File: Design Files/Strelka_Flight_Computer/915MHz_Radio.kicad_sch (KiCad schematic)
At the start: 4 parts

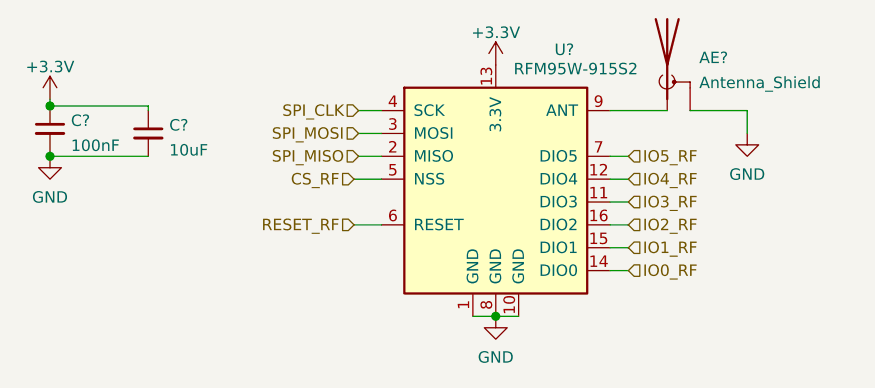
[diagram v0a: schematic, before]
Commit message: Working SPICE sim for ematch continuity circuit
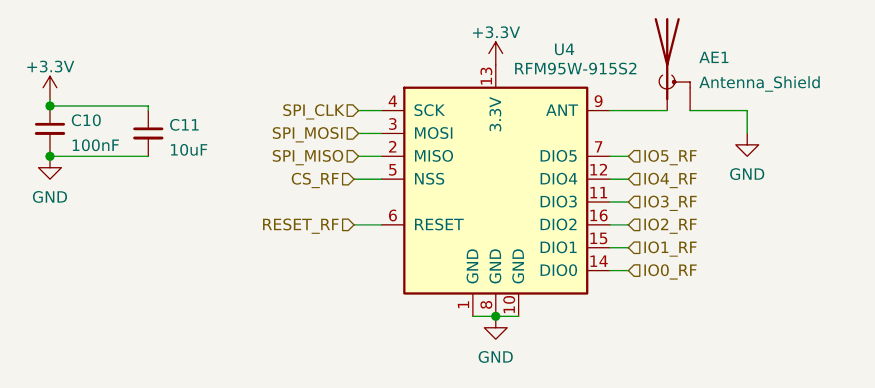
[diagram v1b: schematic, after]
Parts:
- gave numbers to parts that had none: 4
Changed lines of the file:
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@@
   (symbol (lib_id "power:GND") (at 175.26 90.805 0) (unit 1)
     (in_bom yes) (on_board yes) (fields_autoplaced)
-    (property "Reference" "#PWR?" (id 0) (at 175.26 97.155 0)
+    (property "Reference" "#PWR0125" (id 0) (at 175.26 97.155 0)
       (effects (font (size 1.27 1.27)) hide)
     )
@@
   (symbol (lib_id "RF_Module:RFM95W-915S2") (at 147.32 95.885 0) (unit 1)
     (in_bom yes) (on_board yes)
-    (property "Reference" "U?" (id 0) (at 154.94 81.5044 0))
+    (property "Reference" "U4" (id 0) (at 154.94 81.5044 0))
     (property "Value" "RFM95W-915S2" (id 1) (at 156.21 83.6445 0))
     (property "Footprint" "RF_Module:HOPERF_RFM9XW_SMD" (id 2) (at 63.5 53.975 0)
@@
   (symbol (lib_id "Device:C_Small") (at 108.712 90.805 0) (unit 1)
     (in_bom yes) (on_board yes) (fields_autoplaced)
-    (property "Reference" "C?" (id 0) (at 111.0362 89.8965 0)
+    (property "Reference" "C11" (id 0) (at 111.0362 89.8965 0)
       (effects (font (size 1.27 1.27)) (justify left))
     )
@@
   (symbol (lib_id "Device:Antenna_Shield") (at 166.37 83.185 0) (unit 1)
     (in_bom yes) (on_board yes) (fields_autoplaced)
-    (property "Reference" "AE?" (id 0) (at 169.9261 82.4035 0)
+    (property "Reference" "AE1" (id 0) (at 169.9261 82.4035 0)
       (effects (font (size 1.27 1.27)) (justify left))
     )
@@
   (symbol (lib_id "power:+3.3V") (at 147.32 83.185 0) (unit 1)
     (in_bom yes) (on_board yes) (fields_autoplaced)
-    (property "Reference" "#PWR?" (id 0) (at 147.32 86.995 0)
+    (property "Reference" "#PWR0123" (id 0) (at 147.32 86.995 0)
       (effects (font (size 1.27 1.27)) hide)
     )
@@
   (symbol (lib_id "power:+3.3V") (at 97.79 86.995 0) (unit 1)
     (in_bom yes) (on_board yes) (fields_autoplaced)
-    (property "Reference" "#PWR?" (id 0) (at 97.79 90.805 0)
+    (property "Reference" "#PWR0122" (id 0) (at 97.79 90.805 0)
       (effects (font (size 1.27 1.27)) hide)
     )
@@
   (symbol (lib_id "power:GND") (at 147.32 111.125 0) (unit 1)
     (in_bom yes) (on_board yes) (fields_autoplaced)
-    (property "Reference" "#PWR?" (id 0) (at 147.32 117.475 0)
+    (property "Reference" "#PWR0124" (id 0) (at 147.32 117.475 0)
       (effects (font (size 1.27 1.27)) hide)
     )
@@
   (symbol (lib_id "Device:C_Small") (at 97.79 90.297 0) (unit 1)
     (in_bom yes) (on_board yes) (fields_autoplaced)
-    (property "Reference" "C?" (id 0) (at 100.1142 89.3885 0)
+    (property "Reference" "C10" (id 0) (at 100.1142 89.3885 0)
       (effects (font (size 1.27 1.27)) (justify left))
     )
@@
   (symbol (lib_id "power:GND") (at 97.79 93.345 0) (unit 1)
     (in_bom yes) (on_board yes) (fields_autoplaced)
-    (property "Reference" "#PWR?" (id 0) (at 97.79 99.695 0)
+    (property "Reference" "#PWR0126" (id 0) (at 97.79 99.695 0)
       (effects (font (size 1.27 1.27)) hide)
     )

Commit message: Started component placement
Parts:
- AE1: footprint Connector_Coaxial:SMA_Amphenol_132289_EdgeMount -> Connector_Coaxial:SMA_Amphenol_132134_Vertical
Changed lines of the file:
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@@
       (effects (font (size 1.27 1.27)) (justify left))
     )
-    (property "Footprint" "Connector_Coaxial:SMA_Amphenol_132289_EdgeMount" (id 2) (at 166.37 80.645 0)
+    (property "Footprint" "Connector_Coaxial:SMA_Amphenol_132134_Vertical" (id 2) (at 166.37 80.645 0)
       (effects (font (size 1.27 1.27)) hide)
     )

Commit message: Creating BOM
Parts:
- AE1: LCSC C496550 -> (none); LCSC# (none) -> C496550
- U4: LCSC# (none) -> C2844473
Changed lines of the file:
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@@
+      (effects (font (size 1.27 1.27)) hide)
+    )
+    (property "LCSC#" "C2844473" (id 4) (at 147.32 95.885 0)
       (effects (font (size 1.27 1.27)) hide)
     )
@@
       (effects (font (size 1.27 1.27)) hide)
     )
-    (property "LCSC" "C496550" (id 4) (at 166.37 83.185 0)
+    (property "LCSC#" "C496550" (id 4) (at 166.37 83.185 0)
       (effects (font (size 1.27 1.27)) hide)
     )
